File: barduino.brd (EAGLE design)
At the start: 55 x 49.6 mm, 25 parts, among them Q2 16MHz, X1 MINI-USB-UX60A-MB-5ST

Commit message: made the routing pretty(ier)
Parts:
- moved S0 1.88 mm to (17.3, 54.4)
- moved S1 1.82 mm to (4.32, 54.4)
- moved R3 0.52 mm to (5.25, 14.0)
- moved R2 0.13 mm to (11.7, 14.0)
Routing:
- net RESET: track 107.7 -> 104.0 mm
- net N$5: track 57.9 -> 54.7 mm
- net GND: track 114.7 -> 116.3 mm
- net MOSI-D11: track 28.0 -> 27.0 mm
- net D1: track 16.3 -> 15.4 mm
- net D9: track 13.1 -> 13.7 mm
- net N$4: track 5.02 -> 5.55 mm
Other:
- board size 55 x 49.6 mm -> 54.9 x 47.4 mm

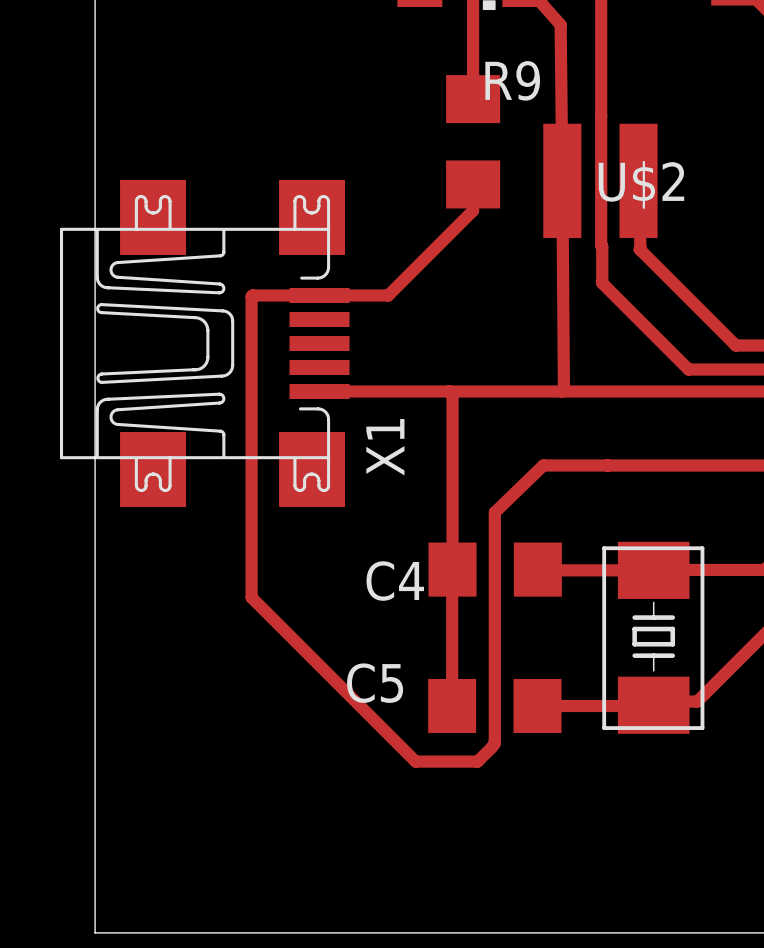
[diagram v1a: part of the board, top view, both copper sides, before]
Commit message: Put new USB power connector on sch/brd
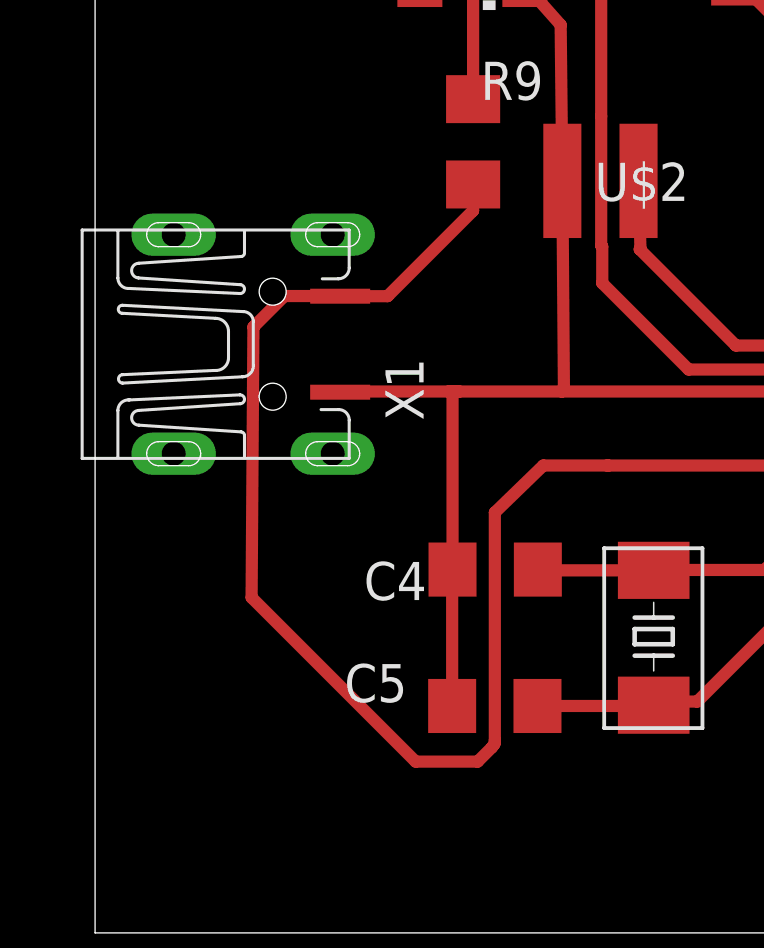
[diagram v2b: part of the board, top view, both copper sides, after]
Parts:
- X1: value MINI-USB-UX60A-MB-5ST -> MINI-USB-PWR; device con-hirose:UX60A-MB-5ST -> 4-Digit-Clock:UX60-MB-5S8-PWR
- moved X1 5.71 mm to (-20.3, 31.9)
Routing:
- net VCC: track 111.4 -> 110.8 mm
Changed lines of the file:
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@@
 <element name="U$2" library="4-Digit-Clock" package="HEADER" value="HEADER" x="10.8103" y="36.7183"/>
 <element name="U$3" library="4-Digit-Clock" package="HEADER" value="HEADER" x="10.8103" y="21.4783" rot="R180"/>
-<element name="X1" library="con-hirose" package="UX60A-MB-5ST" value="MINI-USB-UX60A-MB-5ST" x="-14.5796" y="31.9659">
-<attribute name="MF" value="" x="-14.5796" y="31.9659" size="1.778" layer="27" display="off"/>
-<attribute name="MPN" value="" x="-14.5796" y="31.9659" size="1.778" layer="27" display="off"/>
-<attribute name="OC_FARNELL" value="unknown" x="-14.5796" y="31.9659" size="1.778" layer="27" display="off"/>
-<attribute name="OC_NEWARK" value="unknown" x="-14.5796" y="31.9659" size="1.778" layer="27" display="off"/>
-</element>
 <element name="U$4" library="4-Digit-Clock" package="BUZZER" value="BUZZER" x="-2.96671875" y="37.3862625" rot="R180"/>
 <element name="R1" library="resistor" package="R1206" value="" x="17.820640625" y="13.97"/>
@@
 <element name="R7" library="resistor" package="R1206" value="" x="17.782540625" y="45.2882" rot="R180"/>
 <element name="R8" library="resistor" package="R1206" value="" x="20.614640625" y="37.693603125" rot="R90"/>
+<element name="X1" library="4-Digit-Clock" package="UX60-MB-5S8-PWR" value="MINI-USB-PWR" x="-20.29205625" y="31.94304375"/>
 </elements>
 <signals>
@@
 <wire x1="9.244540625" y1="27.8983" x2="9.922509375" y2="28.57626875" width="0.4064" layer="1"/>
 <contactref element="R9" pad="2"/>
-<contactref element="X1" pad="1"/>
 <wire x1="-2.698959375" y1="27.8983" x2="6.5177" y2="27.8983" width="0.4064" layer="1"/>
-<wire x1="-14.564559375" y1="33.5659" x2="-12.3296" y2="33.5659" width="0.4064" layer="1"/>
-<wire x1="-14.564559375" y1="33.5659" x2="-14.594840625" y2="33.53561875" width="0.4064" layer="1"/>
-<wire x1="-14.594840625" y1="33.53561875" x2="-14.594840625" y2="23.497540625" width="0.4064" layer="1"/>
-<wire x1="-14.594840625" y1="23.497540625" x2="-9.12621875" y2="18.02891875" width="0.4064" layer="1"/>
+<wire x1="-14.53388125" y1="32.517078125" x2="-13.5003" y2="33.54811875" width="0.4064" layer="1"/>
+<wire x1="-14.53388125" y1="32.517078125" x2="-14.594840625" y2="23.497540625" width="0.4064" layer="1"/>
+<wire x1="-9.12621875" y1="18.02891875" x2="-14.594840625" y2="23.497540625" width="0.4064" layer="1"/>
 <wire x1="-9.12621875" y1="18.02891875" x2="-7.0586625" y2="18.02891875" width="0.4064" layer="1"/>
 <wire x1="-7.0586625" y1="18.02891875" x2="-6.58368125" y2="18.5039" width="0.4064" layer="1"/>
@@
 <wire x1="-4.87171875" y1="27.899359375" x2="-2.748278125" y2="27.899359375" width="0.4064" layer="1"/>
 <wire x1="-2.748278125" y1="27.899359375" x2="-2.698959375" y2="27.8983" width="0.4064" layer="1"/>
-<wire x1="-10.03828125" y1="33.5659" x2="-12.3296" y2="33.5659" width="0.4064" layer="1"/>
 <wire x1="-7.21111875" y1="37.26726875" x2="-7.21111875" y2="36.3930625" width="0.4064" layer="1"/>
-<wire x1="-7.21111875" y1="36.3930625" x2="-10.03828125" y2="33.5659" width="0.4064" layer="1"/>
+<wire x1="-10.0611375" y1="33.54304375" x2="-7.21111875" y2="36.3930625" width="0.4064" layer="1"/>
 <contactref element="LED1" pad="A"/>
 <wire x1="27.107053125" y1="43.9318375" x2="27.107053125" y2="40.388365625" width="0.4064" layer="1"/>
@@
 <wire x1="29.771340625" y1="28.669596875" x2="29.758696875" y2="28.783840625" width="0.4064" layer="1"/>
 <wire x1="29.758696875" y1="28.783840625" x2="29.758696875" y2="31.727253125" width="0.4064" layer="1"/>
+<contactref element="X1" pad="1"/>
+<wire x1="-13.5003" y1="33.54811875" x2="-11.748740625" y2="33.54811875" width="0.4064" layer="1"/>
+<wire x1="-11.748740625" y1="33.54811875" x2="-11.64205625" y2="33.54304375" width="0.4064" layer="1"/>
+<wire x1="-11.64205625" y1="33.54304375" x2="-10.0611375" y2="33.54304375" width="0.4064" layer="1"/>
 </signal>
 <signal name="GND" class="1">
@@
 <wire x1="19.705265625" y1="29.849740625" x2="19.64430625" y2="30.04814375" width="0.4064" layer="1"/>
 <wire x1="4.64058125" y1="30.177740625" x2="4.64058125" y2="28.71110625" width="0.4064" layer="1"/>
-<contactref element="X1" pad="5"/>
 <wire x1="6.5177" y1="28.6983" x2="4.6533875" y2="28.6983" width="0.4064" layer="1"/>
 <wire x1="4.6533875" y1="28.6983" x2="4.64058125" y2="28.71110625" width="0.4064" layer="1"/>
-<wire x1="-8.016240625" y1="30.3659" x2="-12.3296" y2="30.3659" width="0.4064" layer="1"/>
-<wire x1="-8.016240625" y1="30.3659" x2="-4.254496875" y2="30.3659" width="0.4064" layer="1"/>
+<wire x1="-4.254496875" y1="30.3659" x2="-7.67588125" y2="30.3659" width="0.4064" layer="1"/>
+<wire x1="-7.67588125" y1="30.3659" x2="-8.016240625" y2="30.3659" width="0.4064" layer="1"/>
 <wire x1="4.452421875" y1="30.3659" x2="4.64058125" y2="30.177740625" width="0.4064" layer="1"/>
 <wire x1="-7.8964" y1="24.42978125" x2="-7.8964" y2="30.246059375" width="0.4064" layer="1"/>
@@
 <wire x1="25.26538125" y1="39.227759375" x2="25.26538125" y2="45.292534375" width="0.4064" layer="1"/>
 <wire x1="25.26538125" y1="45.292534375" x2="19.65190625" y2="50.906009375" width="0.4064" layer="1"/>
+<contactref element="X1" pad="5"/>
+<wire x1="-7.67588125" y1="30.3659" x2="-11.6192" y2="30.3659" width="0.4064" layer="1"/>
+<wire x1="-11.6192" y1="30.3659" x2="-11.64205625" y2="30.34304375" width="0.4064" layer="1"/>
 </signal>
 <signal name="PB7">
@@
 </board>
 </drawing>
+<compatibility>
+<note version="8.3" severity="warning">
+Since Version 8.3, EAGLE supports URNs for individual library
+assets (packages, symbols, and devices). The URNs of those assets
+will not be understood (or retained) with this version.
+</note>
+</compatibility>
 </eagle>

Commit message: Buttons don't have a value
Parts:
- S0: value HR -> (none)
- S1: value MIN -> (none)
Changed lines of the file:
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@@
 <attribute name="VALUE" x="-9.62411875" y="40.08626875" size="1.27" layer="27" rot="R270"/>
 </element>
-<element name="S0" library="ng" package="6MM_SWITCH" value="HR" x="17.272" y="54.356" smashed="yes" rot="R90">
+<element name="S0" library="ng" package="6MM_SWITCH" value="" x="17.272" y="54.356" smashed="yes" rot="R90">
 <attribute name="VALUE" x="22.352" y="51.308" size="1.27" layer="27" ratio="10" rot="R90"/>
 </element>
@@
 <element name="U$1" library="fab" package="TQFP32-08THIN" value="ATMEGA88-THIN" x="10.8103" y="29.0983"/>
 <element name="ICSP" library="fab" package="2X03SMD" value="PROG" x="28.514096875" y="27.335546875" rot="R90"/>
-<element name="S1" library="ng" package="6MM_SWITCH" value="MIN" x="4.318" y="54.356" rot="R90"/>
+<element name="S1" library="ng" package="6MM_SWITCH" value="" x="4.318" y="54.356" rot="R90"/>
 <element name="U$2" library="4-Digit-Clock" package="HEADER" value="HEADER" x="10.8103" y="36.7183"/>
 <element name="U$3" library="4-Digit-Clock" package="HEADER" value="HEADER" x="10.8103" y="21.4783" rot="R180"/>

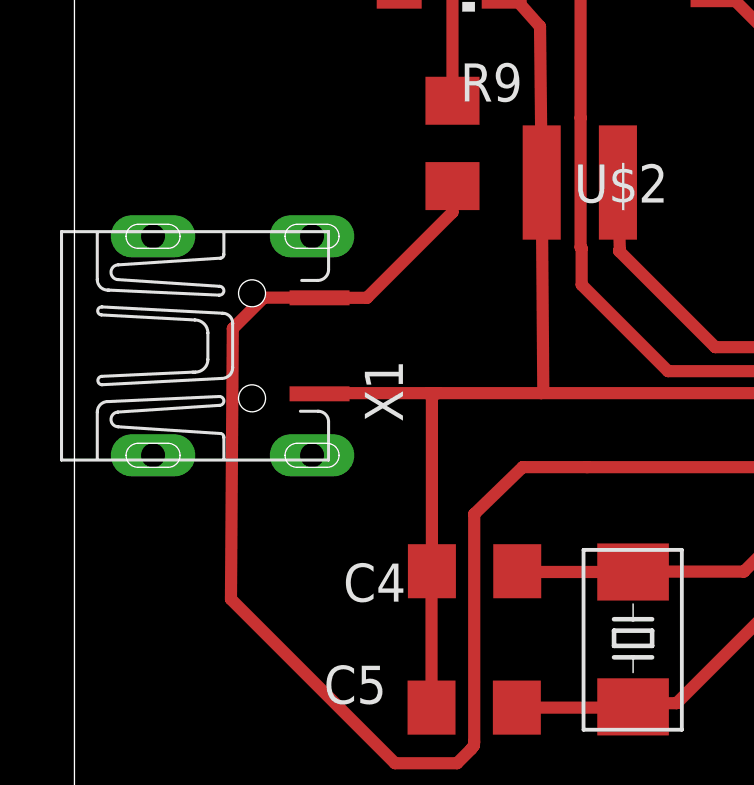
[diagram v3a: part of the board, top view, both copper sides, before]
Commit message: replace thru hole (mistake) with surface mount USB connector
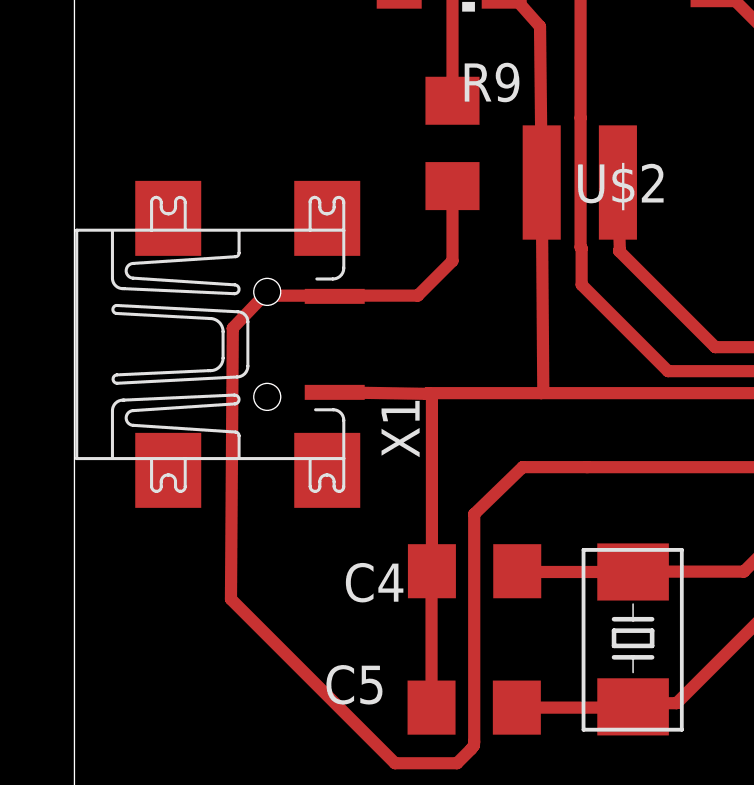
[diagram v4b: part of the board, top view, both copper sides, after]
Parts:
- X1: device 4-Digit-Clock:UX60-MB-5S8-PWR -> 4-Digit-Clock:UX60-MB-5ST-PWR
- moved X1 6.91 mm to (-13.4, 32.0)
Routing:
- net VCC: track 110.8 -> 111.8 mm
- net GND: track 116.0 -> 115.1 mm
